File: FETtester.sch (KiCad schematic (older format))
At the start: 40 parts, among them J1 Conn_01x06_Male, J2 Conn_02x03_Counter_Clockwise, Q1 MMSS8050, Q2 BF862, U1 LMC6044, U2 LMC6044, U3 LM324, U4 AD7249ARZ, U5 LM7705, U6 LDK320ADU120R

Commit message: Added negative swing on gate-source bias and RTD connection.
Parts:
- removed C12: 0.1uF, Capacitor_SMD:C_0603_1608Metric, symbol Device:C
- removed C14, C15: DNP, Capacitor_SMD:C_0603_1608Metric, symbol Device:C
- removed C17: 4.7uF, Capacitor_SMD:C_0603_1608Metric, symbol Device:C
- removed C18: 0.47uF, Capacitor_SMD:C_0603_1608Metric, symbol Device:C
- removed U4: AD7249ARZ, Package_SO:SOIC-16W_7.5x10.3mm_P1.27mm, symbol 2020-08-04_15-28-55:AD7249ARZ
- removed U5: LM7705, Package_SO:VSSOP-8_3.0x3.0mm_P0.65mm, symbol Regulator_SwitchedCapacitor:LM7705
- removed U6: LDK320ADU120R, Package_TO_SOT_SMD:SOT-89-3, symbol Regulator_Linear:HT75xx-1-SOT89
- added J3: RTD, FETtester:DIN_4, symbol Connector_Generic:Conn_02x02_Counter_Clockwise
- added R50: 787, Resistor_SMD:R_0603_1608Metric, symbol Device:R
- added R51: 12.4k, Resistor_SMD:R_0603_1608Metric, symbol Device:R
- added R52, R53, R54, R55, R59: 10k, Resistor_SMD:R_0603_1608Metric, symbol Device:R
- added R56: 3.32k, Resistor_SMD:R_0603_1608Metric, symbol Device:R
- added R57: 339, Resistor_SMD:R_0603_1608Metric, symbol Device:R
- added R58: 2.8k, Resistor_SMD:R_0603_1608Metric, symbol Device:R
- added R60: 100k, Resistor_SMD:R_0603_1608Metric, symbol Device:R
- added U4: LM324, Package_SO:SOIC-14_3.9x8.7mm_P1.27mm, symbol Amplifier_Operational:LM324
- added U5: AD5687, Package_SO:TSSOP-16_4.4x5mm_P0.65mm, symbol Analog_DAC:AD5687BRUZ
- added U6: LTC1983, Package_TO_SOT_SMD:TSOT-23-6, symbol LTC1983:LTC1983
- added U7: L78L10, Package_TO_SOT_SMD:SOT-89-3, symbol Regulator_Linear:L78L10_SOT89
- C11, C16: value 22uF -> 10uF
- C13: value 4.7uF -> 1uF
- C19, C20: value 1uF -> 10uF
- C8: value 0.1uF -> 10uF
- J1: value Conn_01x06_Male -> FET; footprint Connector_PinHeader_2.54mm:PinHeader_1x06_P2.54mm_Vertical -> Connector_PinHeader_2.54mm:PinHeader_1x08_P2.54mm_Vertical; symbol Connector:Conn_01x06_Male -> Connector:Conn_01x08_Male
- R6, R8, R9: value 50 -> 10k
- R7: value 50 -> DNP
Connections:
- net CLR* is gone; now on net LDAC*: A1.22 (D7)
- net +10V: now also C7.2, U4.4 (V+), U7.1 (OUT); no longer C9.1, R3.1
- net +3V3: now also R54.2
- net +5V: now also C8.1, C9.2, R51.1, U5.10 (GAIN), U5.11 (VLOGIC), U5.5 (VDD), U6.1 (Vin), U6.6 (SHDN*); no longer C10.1
- net DACVd: now also U4.1; no longer C8.1
- net GND: now also C10.1, C7.1, C9.1, J1.1 (Pin_1), J1.8 (Pin_8), R7.2, R8.1, R52.2, R56.1, R59.2, U5.16 (RSTSEL), U5.4 (GND), U6.5 (GND), U7.2 (GND); no longer C10.2, C7.2, C9.2, R8.2
- net Id: now also A1.11 (A2); no longer A1.10 (A1)
- net Ig: now also A1.10 (A1); no longer A1.9 (A0)
- net LDAC*: now also U5.9 (~LDAC); no longer A1.20 (D5)
- net MISO: now also U5.8 (SDO)
- net MOSI: now also U5.14 (SDIN)
- net SCK: now also U5.12 (SCLK)
- net SYNC*: now also U5.13 (~SYNC)
- net VIN: now also R3.1, U7.3 (IN)
- net VRg: now also R53.2, U4.7; no longer C7.1, R6.2
- net Vd: now also J1.6 (Pin_6); no longer J1.5 (Pin_5)
- net VdSense: now also J1.7 (Pin_7); no longer J1.6 (Pin_6)
- net Vg: now also J1.2 (Pin_2); no longer J1.1 (Pin_1)
- net VgSense: now also J1.3 (Pin_3); no longer J1.2 (Pin_2)
- net Vgs: now also A1.9 (A0); no longer A1.11 (A2)
- net Vs: now also J1.4 (Pin_4); no longer J1.3 (Pin_3)
- net VsSense: now also J1.5 (Pin_5); no longer J1.4 (Pin_4)
- net at C13.1: now also U6.3 (C+)
- net at C13.2: now also U6.4 (C-)
- net at R6.1, R7.1: now also U4.3 (+)
- net at R9.1: now also R8.2, U4.2 (-)
- net VSS renamed -5V
- net -5V: now also C10.2, U4.11 (V-), U6.2 (Vout)
- new net: R50.1, R52.1, U4.5 (+)
- new net: R51.2, R53.1, U4.6 (-)
- new net: R54.1, U4.10 (+)
- new net: J3.1 (Pin_1), U4.8
- new net: R55.1, U4.9 (-)
- new net: J3.4 (Pin_4), R55.2, R56.2
- new net: R57.1, R59.1, U4.12 (+)
- new net: R58.1, R60.1, U4.13 (-)
- new net: J3.3 (Pin_3), R58.2
- new net: J3.2 (Pin_2), R57.2
- new net DACA: R6.2, U5.3 (VOUTA)
- new net DACB: R50.2, U5.7 (VOUTB)
- new net RESET*: A1.20 (D5), U5.15 (~RESET)
- new net VRTD: R60.2, U4.14
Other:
- note removed: "-0.232V regulated output for opamps."
- moved on the sheet: C11, C13, C16, C8, C9

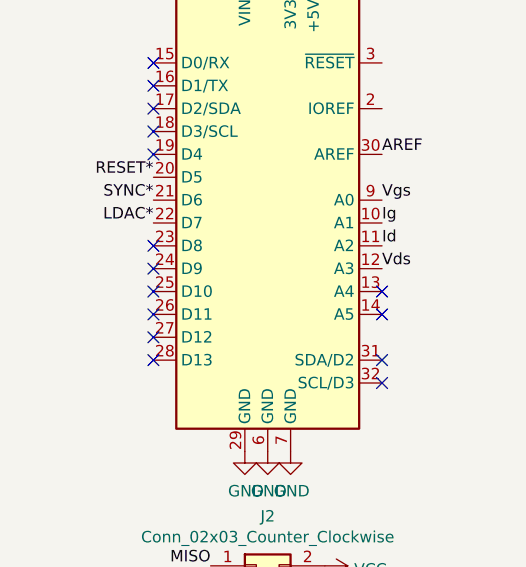
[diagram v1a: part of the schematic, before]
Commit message: Fixed missing connection for RTD line.
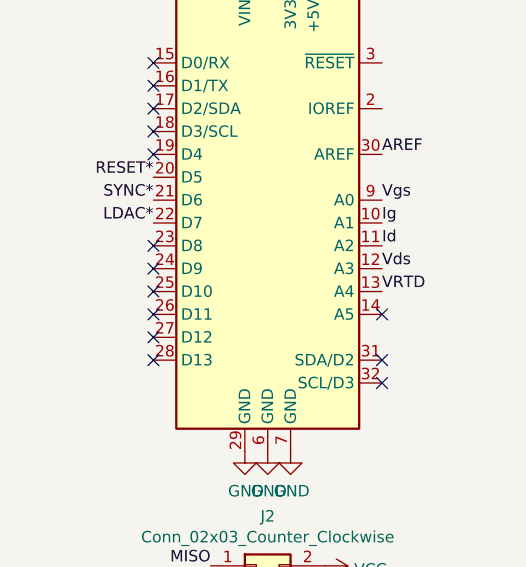
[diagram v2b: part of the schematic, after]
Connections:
- net VRTD: now also A1.13 (A4)
- no-connect marks 15 -> 14
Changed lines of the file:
@@
 	1    0    0    1
 $EndComp
-NoConn ~ 11000 2500
 NoConn ~ 11000 2600
 Wire Wire Line
@@
 	0    -1   -1   0
 $EndComp
+Text Label 11000 2500 0    50   ~ 0
+VRTD
 $EndSCHEMATC
